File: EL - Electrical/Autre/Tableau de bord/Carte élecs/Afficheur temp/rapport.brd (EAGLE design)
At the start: 79 x 42 mm, 25 parts, among them IC1 MCP23008P, IC2 MCP23008P, X1 22-23-2041

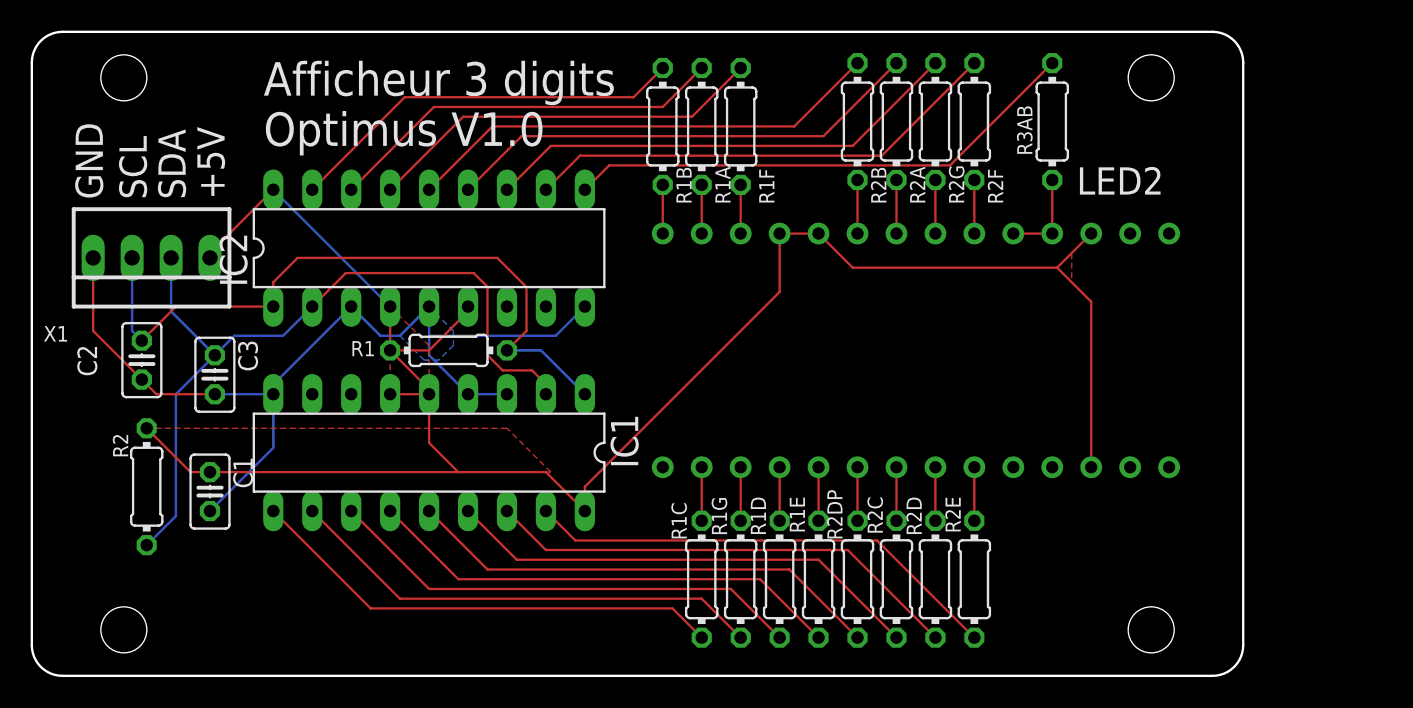
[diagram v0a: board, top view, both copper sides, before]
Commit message: Changement afficheur temp
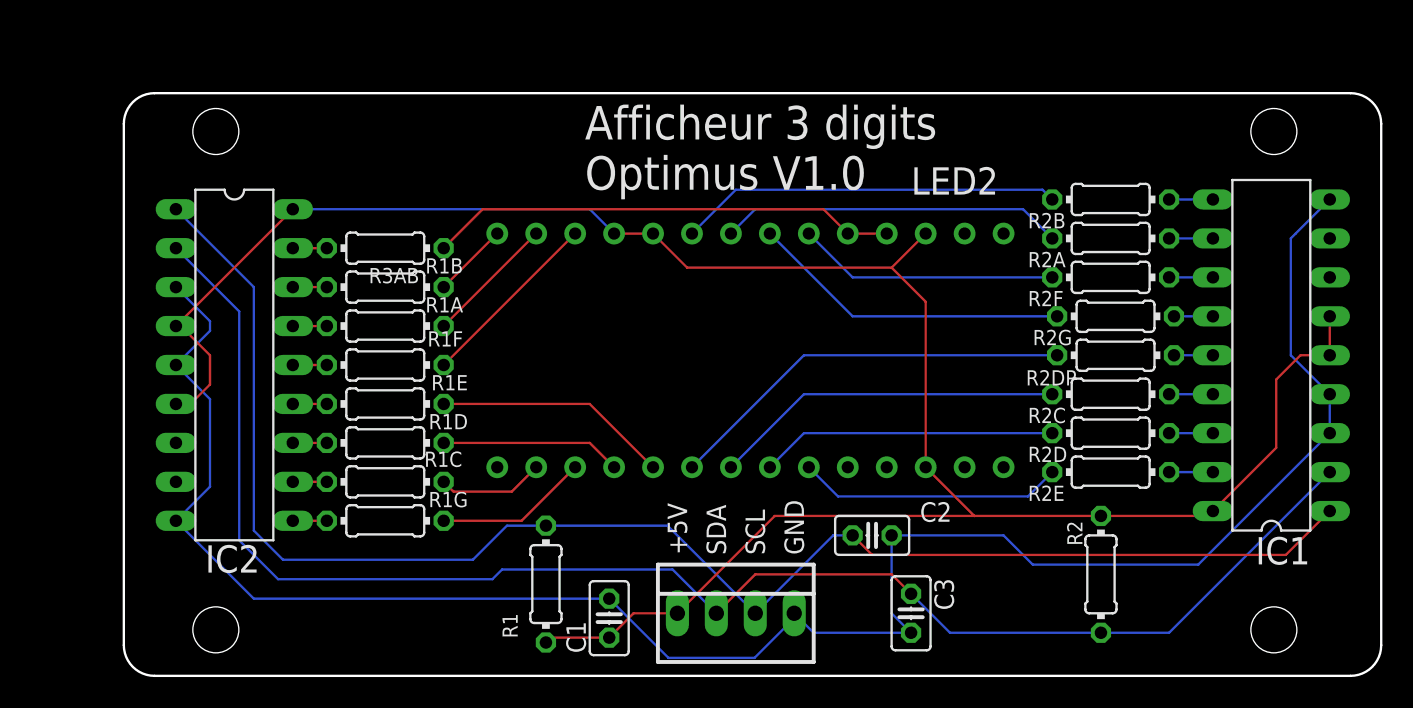
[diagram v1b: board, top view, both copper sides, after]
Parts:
- moved R2 62.5 mm to (65.7, 7.62)
- moved IC1 55.3 mm to (76.8, 21.9), turned to 90 degrees
- moved C2 49.0 mm to (50.8, 10.2), turned to 0 degrees
- moved C3 48.0 mm to (53.3, 5.08)
- moved X1 44.6 mm to (41.9, 5.08), turned to 0 degrees
- moved R3AB 44.3 mm to (19.1, 28.9), turned to 180 degrees
- moved R1E 30.5 mm to (19.1, 18.7), turned to 180 degrees
- moved R1F 27.9 mm to (19.1, 21.3), turned to 180 degrees
- moved C1 27.3 mm to (33.7, 4.76), turned to 90 degrees
- moved R1D 27.2 mm to (19.1, 16.2), turned to 180 degrees
- moved R1A 24.4 mm to (19.1, 23.8), turned to 180 degrees
- moved R1G 23.5 mm to (19.1, 11.1), turned to 180 degrees
- moved R2DP 22.3 mm to (66.7, 21.9), turned to 180 degrees
- moved R1C 21.6 mm to (19.1, 13.7), turned to 180 degrees
- moved R1B 20.9 mm to (19.1, 26.4), turned to 180 degrees
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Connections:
- net GP10: now also R2B.2; no longer R1C.2
- net GP11: now also R2A.2; no longer R1G.2
- net GP12: now also R2F.2; no longer R1D.2
- net GP13: now also R2G.2; no longer R1E.2
- net GP20: now also R1G.2; no longer R3AB.2
- net GP21: now also R1C.2; no longer R2F.2
- net GP22: now also R1D.2; no longer R2G.2
- net GP23: now also R1E.2; no longer R2A.2
- net GP24: now also R1F.2; no longer R2B.2
- net GP25: now also R1A.2; no longer R1F.2
- net GP26: now also R1B.2; no longer R1A.2
- net GP27: now also R3AB.2; no longer R1B.2
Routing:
- net GND: track 63.2 -> 129.5 mm
- net SCL: track 45.6 -> 101.1 mm
- net SDA: track 52.5 -> 101.3 mm
- net GP20: track 33.9 -> 2.22 mm
- net GP23: track 31.4 -> 2.22 mm
- net GP22: track 31.4 -> 2.22 mm
- net GP21: track 31.4 -> 2.22 mm
- net GP24: track 31.4 -> 2.22 mm
- net GP14: track 31.4 -> 2.54 mm
- net GP13: track 31.4 -> 2.54 mm
- net GP17: track 31.4 -> 2.86 mm
- net GP16: track 31.4 -> 2.86 mm
- net GP12: track 31.4 -> 2.86 mm
- net GP15: track 31.4 -> 2.86 mm
- net GP11: track 31.4 -> 2.86 mm
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- removed copper zone on layer 1, net +5V
- removed copper zone on layer 16, net GND
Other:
- board size 79 x 42 mm -> 82 x 38 mm
